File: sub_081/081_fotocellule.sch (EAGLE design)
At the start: 13 parts, among them IC1 TL082P

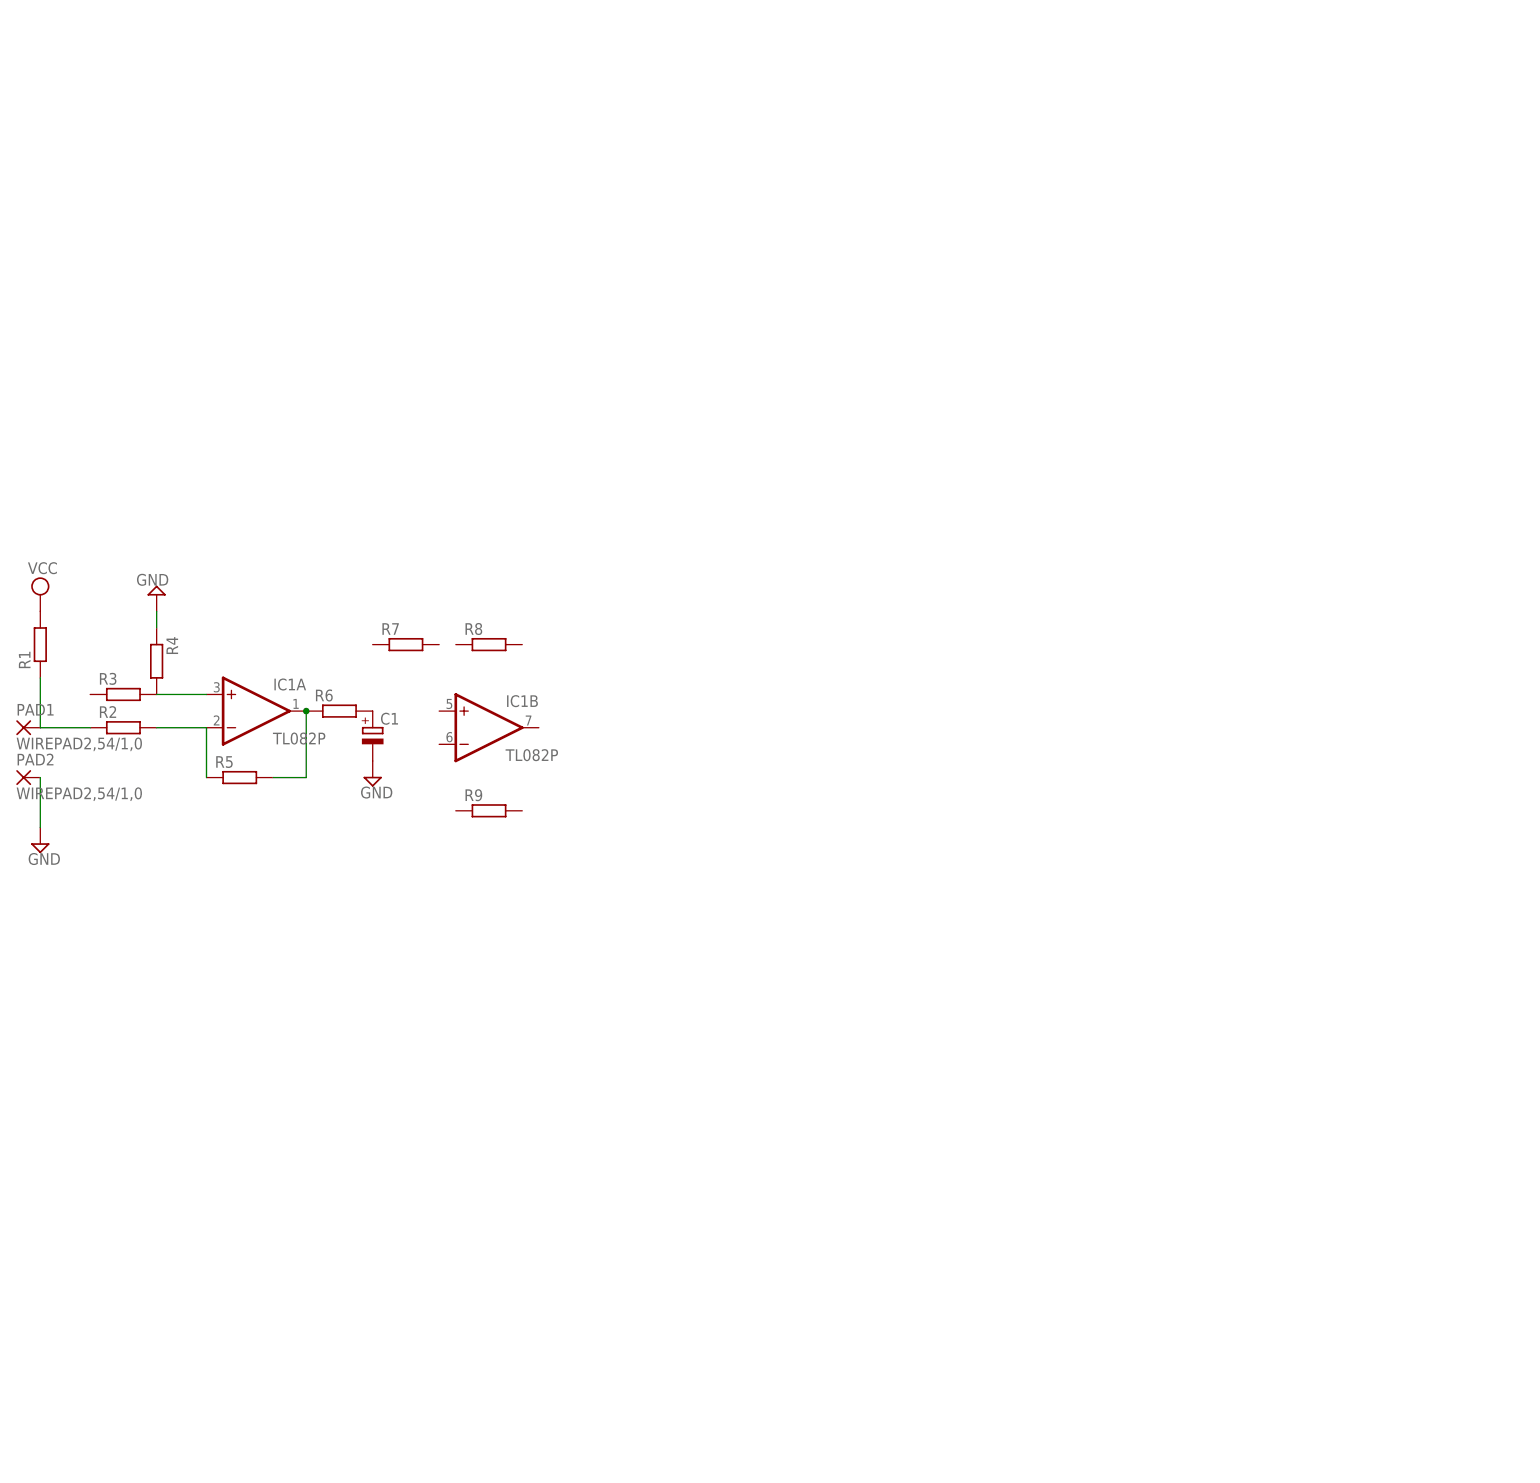
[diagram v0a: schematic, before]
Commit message: Risistemati i due progetti per l'utilizzo dei singoli/doppi opamp
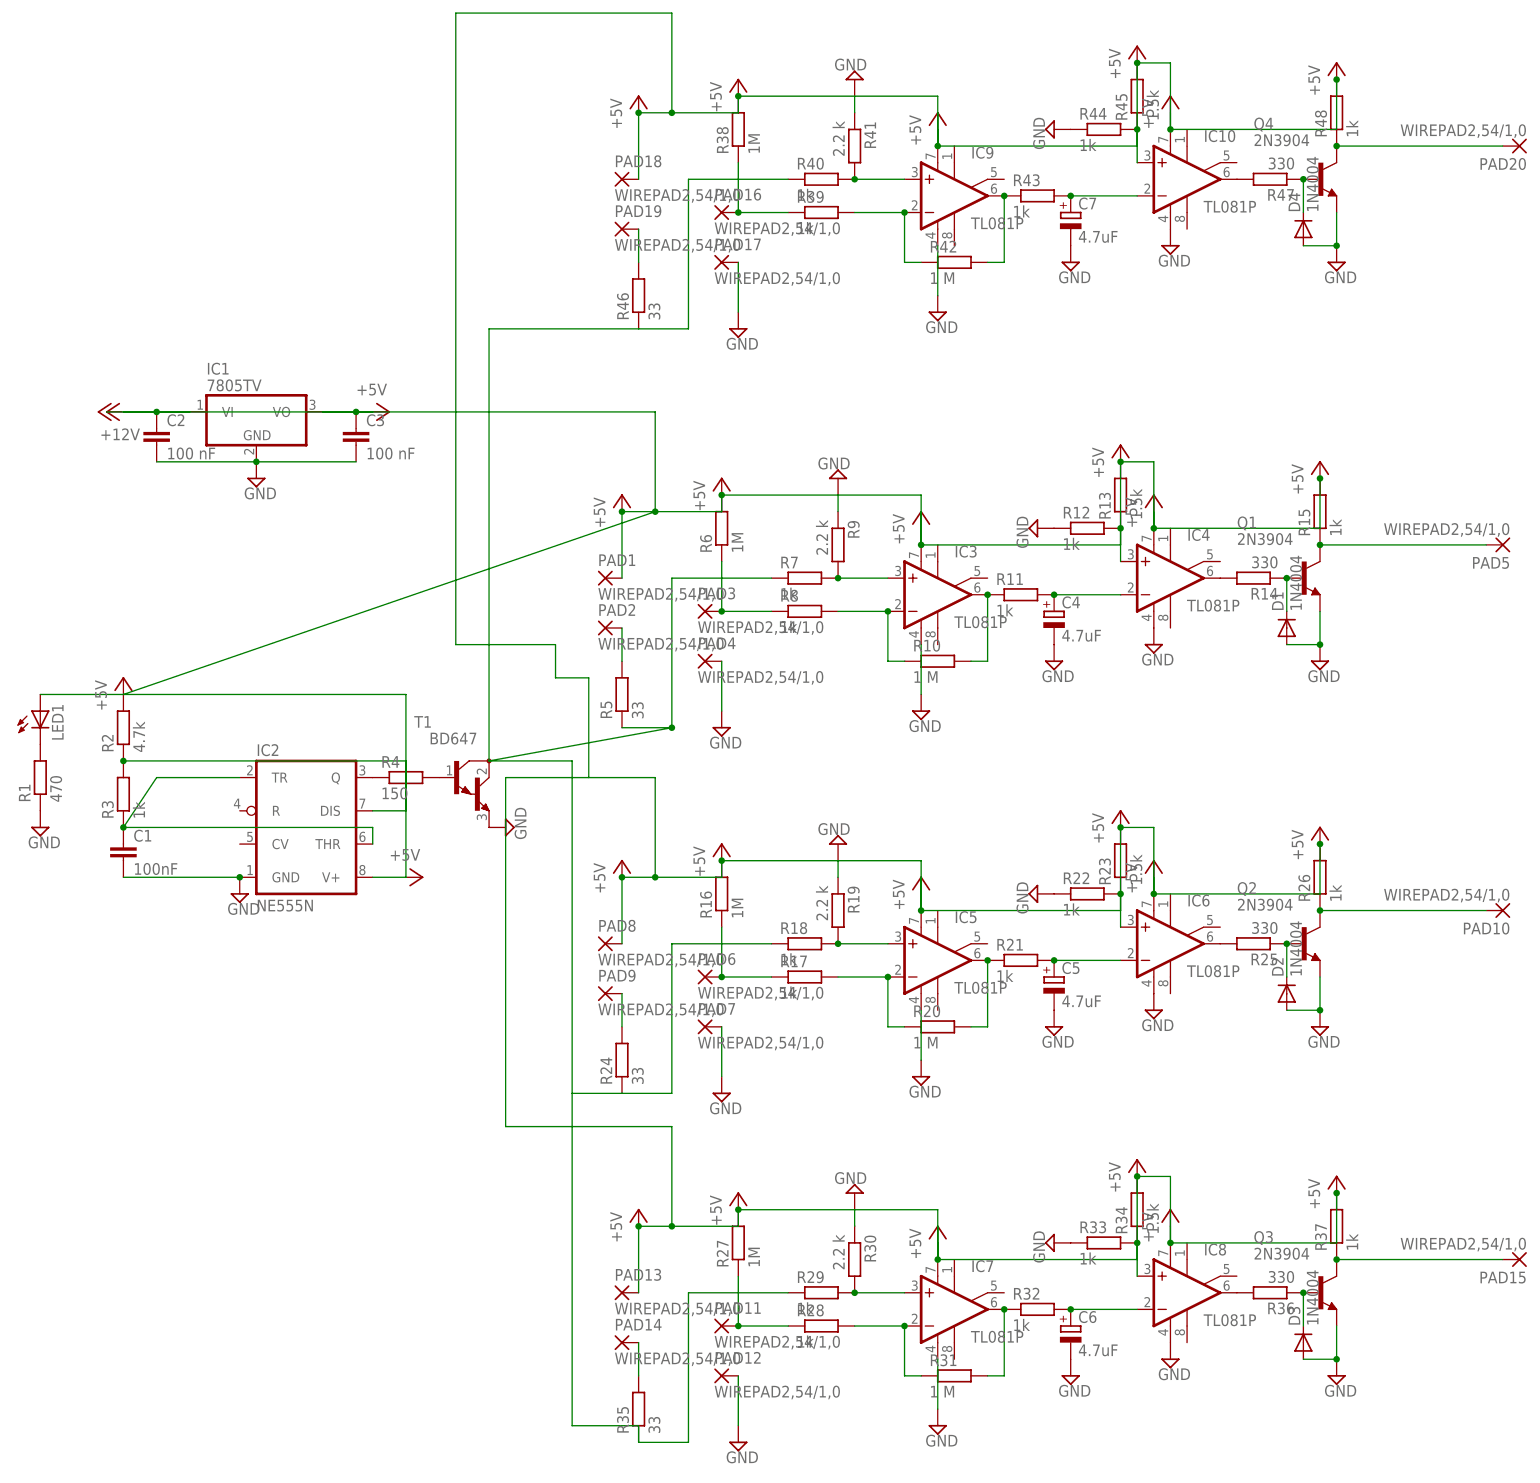
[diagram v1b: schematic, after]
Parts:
- added C2, C3: 100 nF, resistor:C-EU025-024X044
- added C4, C5, C6, C7: 4.7uF, resistor:CPOL-EUE2.5-6
- added D1, D2, D3, D4: 1N4004, diode:1N4004
- added IC10, IC3, IC4, IC5, IC6, IC7, IC8, IC9: TL081P, linear:TL081P
- added IC2: NE555N, linear:NE555N
- added LED1: (no value), led:LED5MM
- added PAD10, PAD11, PAD12, PAD13, PAD14, PAD15, PAD16, PAD17, PAD18, PAD19, PAD20, PAD3, PAD4, PAD5, PAD6, PAD7, PAD8, PAD9: WIREPAD2,54/1,0, wirepad:WIREPAD2,54/1,0
- added Q1, Q2, Q3, Q4: 2N3904, transistor-npn:2N3904
- added R10, R20, R31, R42: 1 M, resistor:R-EU_0207/10
- added R11, R12, R15, R17, R18, R21, R22, R26, R28, R29, R32, R33, R37, R39, R40, R43, R44, R48: 1k, resistor:R-EU_0207/10
- added R13, R23, R34, R45: 1.5k, resistor:R-EU_0207/10
- added R14, R25, R36, R47: 330, resistor:R-EU_0207/10
- added R16, R27, R38: 1M, resistor:R-EU_0207/10
- added R19, R30, R41: 2.2 k, resistor:R-EU_0207/10
- added R24, R35, R46: 33, resistor:R-EU_0207/10
- added T1: BD647, transistor:BD647
- C1: value (none) -> 100nF; device resistor:CPOL-EUE2.5-6 -> resistor:C-EU025-024X044
- IC1: value TL082P -> 7805TV; device linear:TL082P -> linear:7805TV
- R1: value (none) -> 470
- R2: value (none) -> 4.7k
- R3, R7, R8: value (none) -> 1k
- R4: value (none) -> 150
- R5: value (none) -> 33
- R6: value (none) -> 1M
- R9: value (none) -> 2.2 k
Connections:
- new net +5V: C3.1, IC1.VO, IC10.V+, IC2.V+, IC3.V+, IC4.V+, IC5.V+, IC6.V+, IC7.V+, IC8.V+, IC9.V+, LED1.A, PAD1.P, PAD13.P, PAD18.P, PAD8.P, R13.2, R15.2, R16.2, R2.2, R23.2, R26.2, R27.2, R34.2, R37.2, R38.2, R45.2, R48.2, R6.2
- new net N$10: C1.1, IC2.THR, IC2.TR, R3.1
- new net N$11: IC4.OUT, R14.2
- new net N$12: R4.2, T1.B
- new net N$13: IC5.-IN, R17.2, R20.1
- new net N$14: LED1.C, R1.2
- new net N$15: IC2.DIS, R2.1, R3.2
- new net N$16: PAD5.P, Q1.C, R15.1
- new net N$17: IC5.+IN, R18.2, R19.2
- new net N$18: D1.C, Q1.B, R14.1
- new net N$19: IC5.OUT, R20.2, R21.1
- new net N$20: C5.+, IC6.-IN, R21.2
- new net N$21: IC6.+IN, R22.2, R23.1
- new net N$23: PAD9.P, R24.2
- new net N$25: PAD10.P, Q2.C, R26.1
- new net N$26: D2.C, Q2.B, R25.1
- new net N$27: IC6.OUT, R25.2
- new net N$28: PAD11.P, R27.1, R28.1
- new net N$29: IC7.-IN, R28.2, R31.1
- new net N$30: IC7.+IN, R29.2, R30.2
- new net N$31: IC7.OUT, R31.2, R32.1
- new net N$32: C6.+, IC8.-IN, R32.2
- new net N$33: IC8.+IN, R33.2, R34.1
- new net N$34: PAD14.P, R35.2
- new net N$36: PAD15.P, Q3.C, R37.1
- new net N$37: D3.C, Q3.B, R36.1
- new net N$38: IC8.OUT, R36.2
- new net N$39: PAD16.P, R38.1, R39.1
- new net N$40: IC9.-IN, R39.2, R42.1
- new net N$41: IC9.+IN, R40.2, R41.2
- new net N$42: IC9.OUT, R42.2, R43.1
- new net N$43: C7.+, IC10.-IN, R43.2
- new net N$44: IC10.+IN, R44.2, R45.1
- new net N$45: PAD19.P, R46.2
- new net N$46: R18.1, R24.1, R29.1, R35.1, R40.1, R46.1, R5.1, R7.1, T1.C
- new net N$47: PAD20.P, Q4.C, R48.1
- new net N$48: D4.C, Q4.B, R47.1
- new net N$49: IC10.OUT, R47.2
- new net N$6: IC4.+IN, R12.2, R13.1
- new net N$7: PAD2.P, R5.2
- new net N$8: PAD6.P, R16.1, R17.1
- new net N$9: IC2.Q, R4.1
- net GND: now also C1.2, C2.2, C3.2, C4.-, C5.-, C6.-, C7.-, D1.A, D2.A, D3.A, D4.A, IC1.GND, IC10.V-, IC2.GND, IC3.V-, IC4.V-, IC5.V-, IC6.V-, IC7.V-, IC8.V-, IC9.V-, PAD12.P, PAD17.P, PAD4.P, PAD7.P, Q1.E, Q2.E, Q3.E, Q4.E, R1.1, R12.1, R19.1, R22.1, R30.1, R33.1, R41.1, R44.1, R9.1, T1.E; no longer C1.-, PAD2.P, R4.1
- net N$1: now also PAD3.P, R6.1, R8.1; no longer PAD1.P, R1.1, R2.1
- net N$2: now also IC3.-IN, R10.1, R8.2; no longer IC1A.-IN, R2.2, R5.1
- net N$3: now also IC3.+IN, R7.2, R9.2; no longer IC1A.+IN, R3.2, R4.2
- net N$4: now also IC3.OUT, R10.2, R11.1; no longer IC1A.OUT, R5.2, R6.1
- net N$5: now also C4.+, IC4.-IN, R11.2; no longer C1.+, R6.2
- net VCC: now also C2.1, IC1.VI; no longer R1.2
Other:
- moved on the sheet: PAD1, PAD2, R1, R2, R3, R4, R5, R6, R7, R8, R9
